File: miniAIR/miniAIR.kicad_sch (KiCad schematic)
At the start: 14 parts, among them J1 Conn_relay, J2 Conn_HV_IN, J3 Conn_HV_OUT, J4 Conn_pwr, K1 Relay_SPST-NO, Q1 2N7002, U1 LTO150_TB7, U2 LTO150_TB7

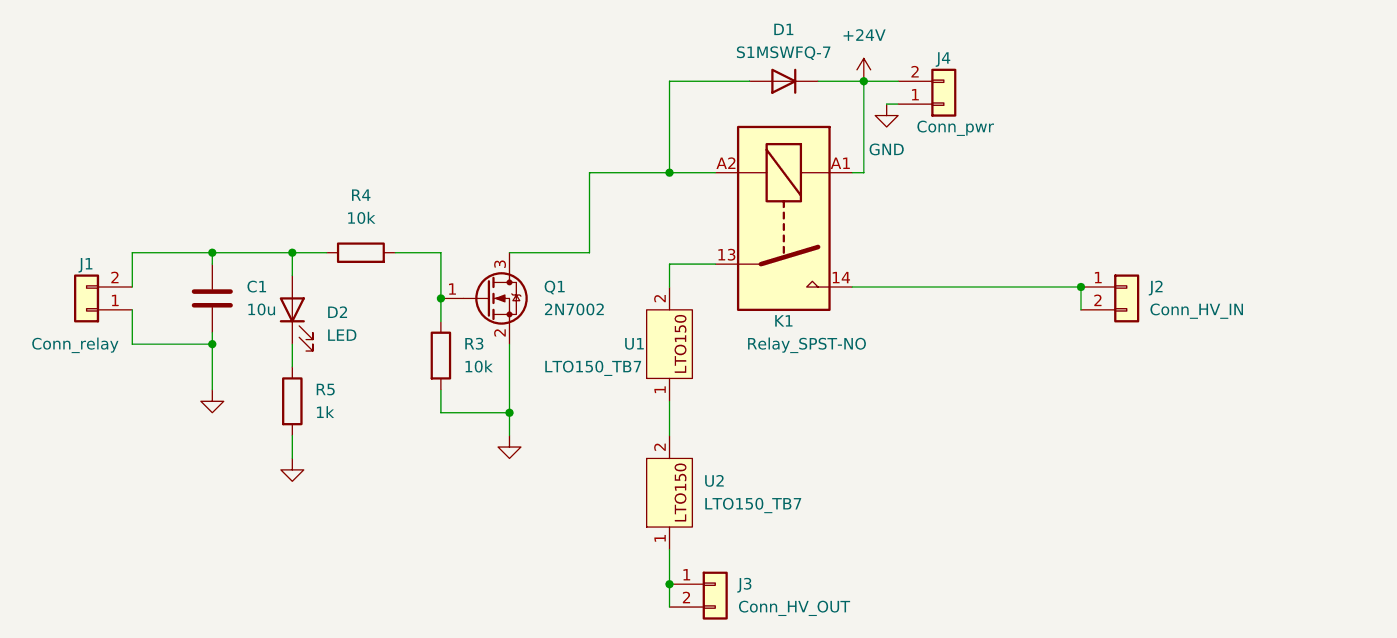
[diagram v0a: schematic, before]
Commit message: fix: reverse the input logic
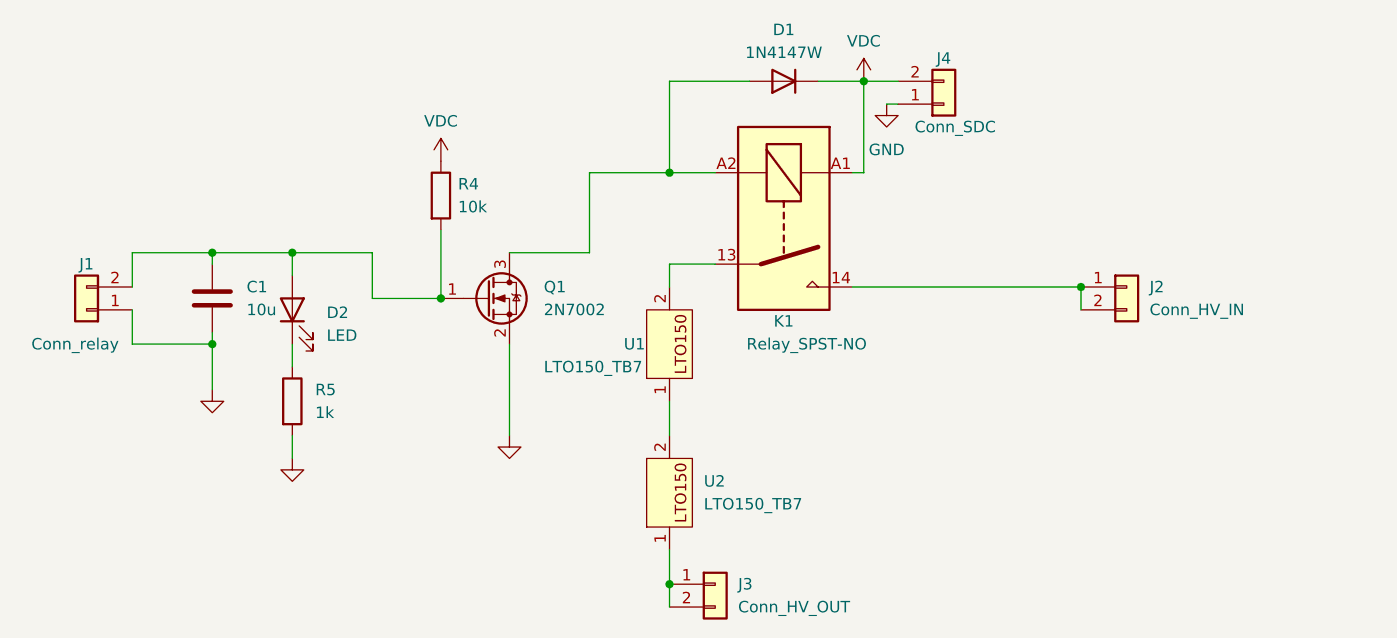
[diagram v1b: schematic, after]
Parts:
- removed R3: 10k, Resistor_SMD:R_0603_1608Metric, symbol Device:R
- D1: value S1MSWFQ-7 -> 1N4147W
- J4: value Conn_pwr -> Conn_SDC
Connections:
- net at Q1.1 (G), R4.2: now also C1.1, D2.2 (A), J1.2 (Pin_2)
- net +24V renamed VDC
- net VDC: now also R4.1
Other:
- moved on the sheet: R4
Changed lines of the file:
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@@
     (company "NCKU Formula Racing")
   )
-  (junction (at 85.09 67.945) (diameter 0) (color 0 0 0 0)
-  )
   (junction (at 102.87 41.275) (diameter 0) (color 0 0 0 0)
   )
@@
   (junction (at 60.96 50.165) (diameter 0) (color 0 0 0 0)
   )
+  (junction (at 52.07 50.165) (diameter 0) (color 0 0 0 0)
+  )
+  (junction (at 148.59 53.975) (diameter 0) (color 0 0 0 0)
+  )
+  (junction (at 52.07 60.325) (diameter 0) (color 0 0 0 0)
+  )
   (junction (at 77.47 55.245) (diameter 0) (color 0 0 0 0)
   )
-  (junction (at 52.07 50.165) (diameter 0) (color 0 0 0 0)
-  )
-  (junction (at 148.59 53.975) (diameter 0) (color 0 0 0 0)
-  )
-  (junction (at 52.07 60.325) (diameter 0) (color 0 0 0 0)
-  )
   (wire (pts (xy 124.46 31.115) (xy 128.27 31.115))
     (stroke (width 0) (type default))
   )
-  (wire (pts (xy 60.96 50.165) (xy 64.77 50.165))
-    (stroke (width 0) (type default))
-  )
-  (wire (pts (xy 72.39 50.165) (xy 77.47 50.165))
-    (stroke (width 0) (type default))
-  )
-  (wire (pts (xy 85.09 67.945) (xy 85.09 70.485))
+  (wire (pts (xy 60.96 50.165) (xy 69.85 50.165))
+    (stroke (width 0) (type default))
+  )
+  (wire (pts (xy 85.09 60.325) (xy 85.09 70.485))
     (stroke (width 0) (type default))
   )
@@
     (stroke (width 0) (type default))
   )
-  (wire (pts (xy 77.47 67.945) (xy 85.09 67.945))
-    (stroke (width 0) (type default))
-  )
   (wire (pts (xy 60.96 52.705) (xy 60.96 50.165))
     (stroke (width 0) (type default))
@@
     (stroke (width 0) (type default))
   )
-  (wire (pts (xy 77.47 65.405) (xy 77.47 67.945))
-    (stroke (width 0) (type default))
-  )
   (wire (pts (xy 148.59 53.975) (xy 148.59 56.515))
     (stroke (width 0) (type default))
@@
     (stroke (width 0) (type default))
   )
+  (wire (pts (xy 69.85 55.245) (xy 77.47 55.245))
+    (stroke (width 0) (type default))
+  )
   (wire (pts (xy 60.96 50.165) (xy 52.07 50.165))
     (stroke (width 0) (type default))
@@
     (stroke (width 0) (type default))
   )
-  (wire (pts (xy 77.47 55.245) (xy 77.47 57.785))
-    (stroke (width 0) (type default))
-  )
-  (wire (pts (xy 77.47 50.165) (xy 77.47 55.245))
-    (stroke (width 0) (type default))
-  )
-  (wire (pts (xy 85.09 60.325) (xy 85.09 67.945))
+  (wire (pts (xy 77.47 47.625) (xy 77.47 55.245))
     (stroke (width 0) (type default))
   )
@@
     (stroke (width 0) (type default))
   )
+  (wire (pts (xy 69.85 50.165) (xy 69.85 55.245))
+    (stroke (width 0) (type default))
+  )
   (wire (pts (xy 102.87 86.995) (xy 102.87 89.535))
     (stroke (width 0) (type default))
@@
     (stroke (width 0) (type default))
   )
-  (symbol (lib_id "Device:R") (at 77.47 61.595 0) (unit 1)
-    (in_bom yes) (on_board yes) (dnp no) (fields_autoplaced)
-    (property "Reference" "R3" (at 80.01 60.325 0)
-      (effects (font (size 1.27 1.27)) (justify left))
-    )
-    (property "Value" "10k" (at 80.01 62.865 0)
-      (effects (font (size 1.27 1.27)) (justify left))
-    )
-    (property "Footprint" "Resistor_SMD:R_0603_1608Metric" (at 75.692 61.595 90)
-      (effects (font (size 1.27 1.27)) hide)
-    )
-    (property "Datasheet" "~" (at 77.47 61.595 0)
-      (effects (font (size 1.27 1.27)) hide)
-    )
-    (pin "2")
-    (pin "1")
-    (instances
-      (project "miniAIR"
-        (path "/6fc1038c-e987-4dec-bdb5-c43600fb1ee3"
-          (reference "R3") (unit 1)
+  (symbol (lib_id "power:VDC") (at 77.47 40.005 0) (unit 1)
+    (in_bom yes) (on_board yes) (dnp no) (fields_autoplaced)
+    (property "Reference" "#PWR06" (at 77.47 42.545 0)
+      (effects (font (size 1.27 1.27)) hide)
+    )
+    (property "Value" "VDC" (at 77.47 35.56 0)
+      (effects (font (size 1.27 1.27)))
+    )
+    (property "Footprint" "" (at 77.47 40.005 0)
+      (effects (font (size 1.27 1.27)) hide)
+    )
+    (property "Datasheet" "" (at 77.47 40.005 0)
+      (effects (font (size 1.27 1.27)) hide)
+    )
+    (pin "1")
+    (instances
+      (project "miniAIR"
+        (path "/6fc1038c-e987-4dec-bdb5-c43600fb1ee3"
+          (reference "#PWR06") (unit 1)
         )
       )
@@
         (path "/6fc1038c-e987-4dec-bdb5-c43600fb1ee3"
           (reference "Q1") (unit 1)
-        )
-      )
-    )
-  )
-  (symbol (lib_id "power:+24V") (at 124.46 31.115 0) (unit 1)
-    (in_bom yes) (on_board yes) (dnp no) (fields_autoplaced)
-    (property "Reference" "#PWR06" (at 124.46 34.925 0)
-      (effects (font (size 1.27 1.27)) hide)
-    )
-    (property "Value" "+24V" (at 124.46 26.035 0)
-      (effects (font (size 1.27 1.27)))
-    )
-    (property "Footprint" "" (at 124.46 31.115 0)
-      (effects (font (size 1.27 1.27)) hide)
-    )
-    (property "Datasheet" "" (at 124.46 31.115 0)
-      (effects (font (size 1.27 1.27)) hide)
-    )
-    (pin "1")
-    (instances
-      (project "miniAIR"
-        (path "/6fc1038c-e987-4dec-bdb5-c43600fb1ee3"
-          (reference "#PWR06") (unit 1)
         )
       )
@@
       (effects (font (size 1.27 1.27)))
     )
-    (property "Value" "Conn_pwr" (at 134.62 36.195 0)
+    (property "Value" "Conn_SDC" (at 134.62 36.195 0)
       (effects (font (size 1.27 1.27)))
     )
@@
     )
   )
-  (symbol (lib_id "Device:R") (at 68.58 50.165 90) (unit 1)
-    (in_bom yes) (on_board yes) (dnp no) (fields_autoplaced)
-    (property "Reference" "R4" (at 68.58 43.815 90)
-      (effects (font (size 1.27 1.27)))
-    )
-    (property "Value" "10k" (at 68.58 46.355 90)
-      (effects (font (size 1.27 1.27)))
-    )
-    (property "Footprint" "Resistor_SMD:R_0603_1608Metric" (at 68.58 51.943 90)
-      (effects (font (size 1.27 1.27)) hide)
-    )
-    (property "Datasheet" "~" (at 68.58 50.165 0)
+  (symbol (lib_id "Device:R") (at 77.47 43.815 0) (unit 1)
+    (in_bom yes) (on_board yes) (dnp no) (fields_autoplaced)
+    (property "Reference" "R4" (at 79.375 42.545 0)
+      (effects (font (size 1.27 1.27)) (justify left))
+    )
+    (property "Value" "10k" (at 79.375 45.085 0)
+      (effects (font (size 1.27 1.27)) (justify left))
+    )
+    (property "Footprint" "Resistor_SMD:R_0603_1608Metric" (at 75.692 43.815 90)
+      (effects (font (size 1.27 1.27)) hide)
+    )
+    (property "Datasheet" "~" (at 77.47 43.815 0)
       (effects (font (size 1.27 1.27)) hide)
     )
@@
     )
   )
+  (symbol (lib_id "power:VDC") (at 124.46 31.115 0) (unit 1)
+    (in_bom yes) (on_board yes) (dnp no) (fields_autoplaced)
+    (property "Reference" "#PWR05" (at 124.46 33.655 0)
+      (effects (font (size 1.27 1.27)) hide)
+    )
+    (property "Value" "VDC" (at 124.46 26.67 0)
+      (effects (font (size 1.27 1.27)))
+    )
+    (property "Footprint" "" (at 124.46 31.115 0)
+      (effects (font (size 1.27 1.27)) hide)
+    )
+    (property "Datasheet" "" (at 124.46 31.115 0)
+      (effects (font (size 1.27 1.27)) hide)
+    )
+    (pin "1")
+    (instances
+      (project "miniAIR"
+        (path "/6fc1038c-e987-4dec-bdb5-c43600fb1ee3"
+          (reference "#PWR05") (unit 1)
+        )
+      )
+    )
+  )
   (symbol (lib_id "Device:D") (at 115.57 31.115 180) (unit 1)
     (in_bom yes) (on_board yes) (dnp no) (fields_autoplaced)
@@
       (effects (font (size 1.27 1.27)))
     )
-    (property "Value" "S1MSWFQ-7" (at 115.57 27.94 0)
-      (effects (font (size 1.27 1.27)))
-    )
+    (property "Value" "1N4147W" (at 115.57 27.94 0)
+      (effects (font (size 1.27 1.27)))
+    )

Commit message: feat: Replace PreC resistor by LPS300
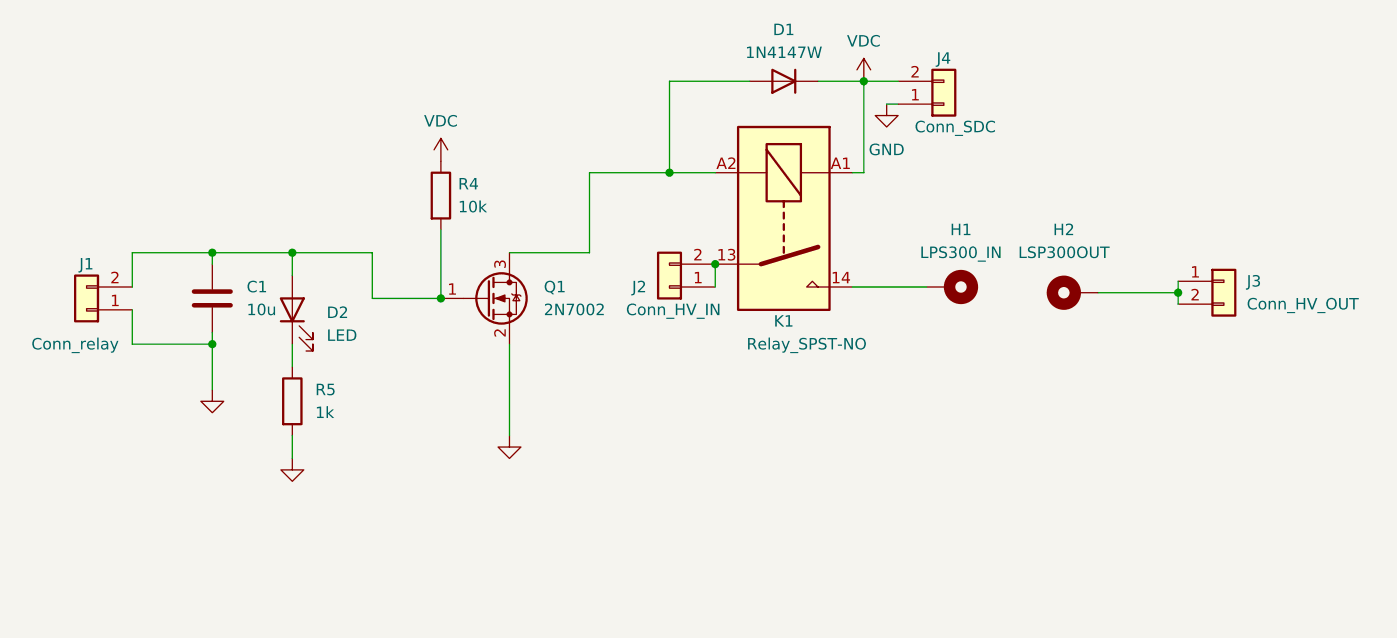
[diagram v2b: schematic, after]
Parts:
- removed U1, U2: LTO150_TB7, Library:LTO150-TB7, symbol custom_Library:LTO150_TB7
- added H1: LPS300_IN, MountingHole:MountingHole_4.3mm_M4_Pad, symbol Mechanical:MountingHole_Pad
- added H2: LSP300OUT, MountingHole:MountingHole_4.3mm_M4_Pad, symbol Mechanical:MountingHole_Pad
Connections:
- net at J2.1 (Pin_1), J2.2 (Pin_2): now also K1.13; no longer K1.14
- net at J3.1 (Pin_1), J3.2 (Pin_2): now also H2.1
- new net: H1.1, K1.14
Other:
- moved on the sheet: J2, J3
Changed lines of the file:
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@@
   (junction (at 124.46 31.115) (diameter 0) (color 0 0 0 0)
   )
-  (junction (at 102.87 86.995) (diameter 0) (color 0 0 0 0)
-  )
   (junction (at 60.96 50.165) (diameter 0) (color 0 0 0 0)
   )
   (junction (at 52.07 50.165) (diameter 0) (color 0 0 0 0)
   )
-  (junction (at 148.59 53.975) (diameter 0) (color 0 0 0 0)
+  (junction (at 159.385 54.61) (diameter 0) (color 0 0 0 0)
+  )
+  (junction (at 107.95 51.435) (diameter 0) (color 0 0 0 0)
   )
   (junction (at 52.07 60.325) (diameter 0) (color 0 0 0 0)
@@
     (stroke (width 0) (type default))
   )
-  (wire (pts (xy 102.87 51.435) (xy 107.95 51.435))
-    (stroke (width 0) (type default))
-  )
-  (wire (pts (xy 102.87 86.995) (xy 102.87 83.185))
-    (stroke (width 0) (type default))
-  )
   (wire (pts (xy 43.18 60.325) (xy 52.07 60.325))
     (stroke (width 0) (type default))
@@
     (stroke (width 0) (type default))
   )
+  (wire (pts (xy 159.385 54.61) (xy 159.385 55.88))
+    (stroke (width 0) (type default))
+  )
   (wire (pts (xy 102.87 31.115) (xy 102.87 41.275))
     (stroke (width 0) (type default))
@@
     (stroke (width 0) (type default))
   )
-  (wire (pts (xy 123.19 53.975) (xy 148.59 53.975))
-    (stroke (width 0) (type default))
-  )
-  (wire (pts (xy 148.59 53.975) (xy 148.59 56.515))
+  (wire (pts (xy 107.95 53.975) (xy 107.95 51.435))
     (stroke (width 0) (type default))
   )
@@
     (stroke (width 0) (type default))
   )
-  (wire (pts (xy 102.87 66.675) (xy 102.87 70.485))
-    (stroke (width 0) (type default))
-  )
   (wire (pts (xy 43.18 50.165) (xy 52.07 50.165))
     (stroke (width 0) (type default))
   )
-  (wire (pts (xy 102.87 53.975) (xy 102.87 51.435))
+  (wire (pts (xy 150.495 54.61) (xy 159.385 54.61))
     (stroke (width 0) (type default))
   )
@@
     (stroke (width 0) (type default))
   )
-  (wire (pts (xy 102.87 86.995) (xy 102.87 89.535))
+  (wire (pts (xy 159.385 53.34) (xy 159.385 54.61))
     (stroke (width 0) (type default))
   )
@@
     (stroke (width 0) (type default))
   )
+  (wire (pts (xy 131.445 53.975) (xy 123.19 53.975))
+    (stroke (width 0) (type default))
+  )
   (wire (pts (xy 128.27 33.655) (xy 127 33.655))
     (stroke (width 0) (type default))
@@
     )
   )
-  (symbol (lib_id "Connector_Generic:Conn_01x02") (at 153.67 53.975 0) (unit 1)
-    (in_bom yes) (on_board yes) (dnp no) (fields_autoplaced)
-    (property "Reference" "J2" (at 156.21 53.975 0)
-      (effects (font (size 1.27 1.27)) (justify left))
-    )
-    (property "Value" "Conn_HV_IN" (at 156.21 56.515 0)
-      (effects (font (size 1.27 1.27)) (justify left))
-    )
-    (property "Footprint" "Connector_Molex:Molex_Micro-Fit_3.0_43650-0200_1x02_P3.00mm_Horizontal" (at 153.67 53.975 0)
-      (effects (font (size 1.27 1.27)) hide)
-    )
-    (property "Datasheet" "~" (at 153.67 53.975 0)
+  (symbol (lib_id "Connector_Generic:Conn_01x02") (at 102.87 53.975 180) (unit 1)
+    (in_bom yes) (on_board yes) (dnp no)
+    (property "Reference" "J2" (at 100.33 53.975 0)
+      (effects (font (size 1.27 1.27)) (justify left))
+    )
+    (property "Value" "Conn_HV_IN" (at 108.585 56.515 0)
+      (effects (font (size 1.27 1.27)) (justify left))
+    )
+    (property "Footprint" "Connector_Molex:Molex_Micro-Fit_3.0_43650-0200_1x02_P3.00mm_Horizontal" (at 102.87 53.975 0)
+      (effects (font (size 1.27 1.27)) hide)
+    )
+    (property "Datasheet" "~" (at 102.87 53.975 0)
       (effects (font (size 1.27 1.27)) hide)
     )
@@
     )
   )
-  (symbol (lib_id "custom_Library:LTO150_TB7") (at 102.87 76.835 90) (unit 1)
-    (in_bom yes) (on_board yes) (dnp no) (fields_autoplaced)
-    (property "Reference" "U2" (at 106.68 75.565 90)
-      (effects (font (size 1.27 1.27)) (justify right))
-    )
-    (property "Value" "LTO150_TB7" (at 106.68 78.105 90)
-      (effects (font (size 1.27 1.27)) (justify right))
-    )
-    (property "Footprint" "Library:LTO150-TB7" (at 102.87 76.835 0)
-      (effects (font (size 1.27 1.27)) hide)
-    )
-    (property "Datasheet" "" (at 102.87 76.835 0)
-      (effects (font (size 1.27 1.27)) hide)
-    )
-    (pin "1")
-    (pin "2")
-    (instances
-      (project "miniAIR"
-        (path "/6fc1038c-e987-4dec-bdb5-c43600fb1ee3"
-          (reference "U2") (unit 1)
+  (symbol (lib_id "Mechanical:MountingHole_Pad") (at 133.985 53.975 270) (mirror x) (unit 1)
+    (in_bom yes) (on_board yes) (dnp no)
+    (property "Reference" "H1" (at 135.255 47.625 90)
+      (effects (font (size 1.27 1.27)))
+    )
+    (property "Value" "LPS300_IN" (at 135.255 50.165 90)
+      (effects (font (size 1.27 1.27)))
+    )
+    (property "Footprint" "MountingHole:MountingHole_4.3mm_M4_Pad" (at 133.985 53.975 0)
+      (effects (font (size 1.27 1.27)) hide)
+    )
+    (property "Datasheet" "~" (at 133.985 53.975 0)
+      (effects (font (size 1.27 1.27)) hide)
+    )
+    (pin "1")
+    (instances
+      (project "miniAIR"
+        (path "/6fc1038c-e987-4dec-bdb5-c43600fb1ee3"
+          (reference "H1") (unit 1)
         )
       )
@@
     )
   )
-  (symbol (lib_id "Connector_Generic:Conn_01x02") (at 107.95 86.995 0) (unit 1)
-    (in_bom yes) (on_board yes) (dnp no) (fields_autoplaced)
-    (property "Reference" "J3" (at 110.49 86.995 0)
-      (effects (font (size 1.27 1.27)) (justify left))
-    )
-    (property "Value" "Conn_HV_OUT" (at 110.49 89.535 0)
-      (effects (font (size 1.27 1.27)) (justify left))
-    )
-    (property "Footprint" "Connector_Molex:Molex_Micro-Fit_3.0_43650-0200_1x02_P3.00mm_Horizontal" (at 107.95 86.995 0)
-      (effects (font (size 1.27 1.27)) hide)
-    )
-    (property "Datasheet" "~" (at 107.95 86.995 0)
+  (symbol (lib_id "Connector_Generic:Conn_01x02") (at 164.465 53.34 0) (unit 1)
+    (in_bom yes) (on_board yes) (dnp no) (fields_autoplaced)
+    (property "Reference" "J3" (at 167.005 53.34 0)
+      (effects (font (size 1.27 1.27)) (justify left))
+    )
+    (property "Value" "Conn_HV_OUT" (at 167.005 55.88 0)
+      (effects (font (size 1.27 1.27)) (justify left))
+    )
+    (property "Footprint" "Connector_Molex:Molex_Micro-Fit_3.0_43650-0200_1x02_P3.00mm_Horizontal" (at 164.465 53.34 0)
+      (effects (font (size 1.27 1.27)) hide)
+    )
+    (property "Datasheet" "~" (at 164.465 53.34 0)
       (effects (font (size 1.27 1.27)) hide)
     )
@@
         (path "/6fc1038c-e987-4dec-bdb5-c43600fb1ee3"
           (reference "J3") (unit 1)
-        )
-      )
-    )
-  )
-  (symbol (lib_name "LTO150_TB7_1") (lib_id "custom_Library:LTO150_TB7") (at 102.87 60.325 90) (unit 1)
-    (in_bom yes) (on_board yes) (dnp no)
-    (property "Reference" "U1" (at 97.79 60.325 90)
-      (effects (font (size 1.27 1.27)) (justify right))
-    )
-    (property "Value" "LTO150_TB7" (at 88.9 62.865 90)
-      (effects (font (size 1.27 1.27)) (justify right))
-    )
-    (property "Footprint" "Library:LTO150-TB7" (at 102.87 60.325 0)
-      (effects (font (size 1.27 1.27)) hide)
-    )
-    (property "Datasheet" "" (at 102.87 60.325 0)
-      (effects (font (size 1.27 1.27)) hide)
-    )
-    (pin "1")
-    (pin "2")
-    (instances
-      (project "miniAIR"
-        (path "/6fc1038c-e987-4dec-bdb5-c43600fb1ee3"
-          (reference "U1") (unit 1)
         )
       )
@@
         )
       )
+    )
+  )
+  (symbol (lib_id "Mechanical:MountingHole_Pad") (at 147.955 54.61 90) (unit 1)
+    (in_bom yes) (on_board yes) (dnp no) (fields_autoplaced)
+    (property "Reference" "H2" (at 146.685 47.625 90)
+      (effects (font (size 1.27 1.27)))
+    )
+    (property "Value" "LSP300OUT" (at 146.685 50.165 90)
+      (effects (font (size 1.27 1.27)))
+    )
+    (property "Footprint" "MountingHole:MountingHole_4.3mm_M4_Pad" (at 147.955 54.61 0)
+      (effects (font (size 1.27 1.27)) hide)
+    )
+    (property "Datasheet" "~" (at 147.955 54.61 0)
+      (effects (font (size 1.27 1.27)) hide)
+    )
+    (pin "1")
+    (instances
+      (project "miniAIR"
+        (path "/6fc1038c-e987-4dec-bdb5-c43600fb1ee3"
+          (reference "H2") (unit 1)
+        )
+      )
